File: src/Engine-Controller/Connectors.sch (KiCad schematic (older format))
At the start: 5 parts, among them P3 SBH11-PBPC-D05-RA-BK, P4 0901471110, P5 66953-005LF, U4 SN74LV07ADR

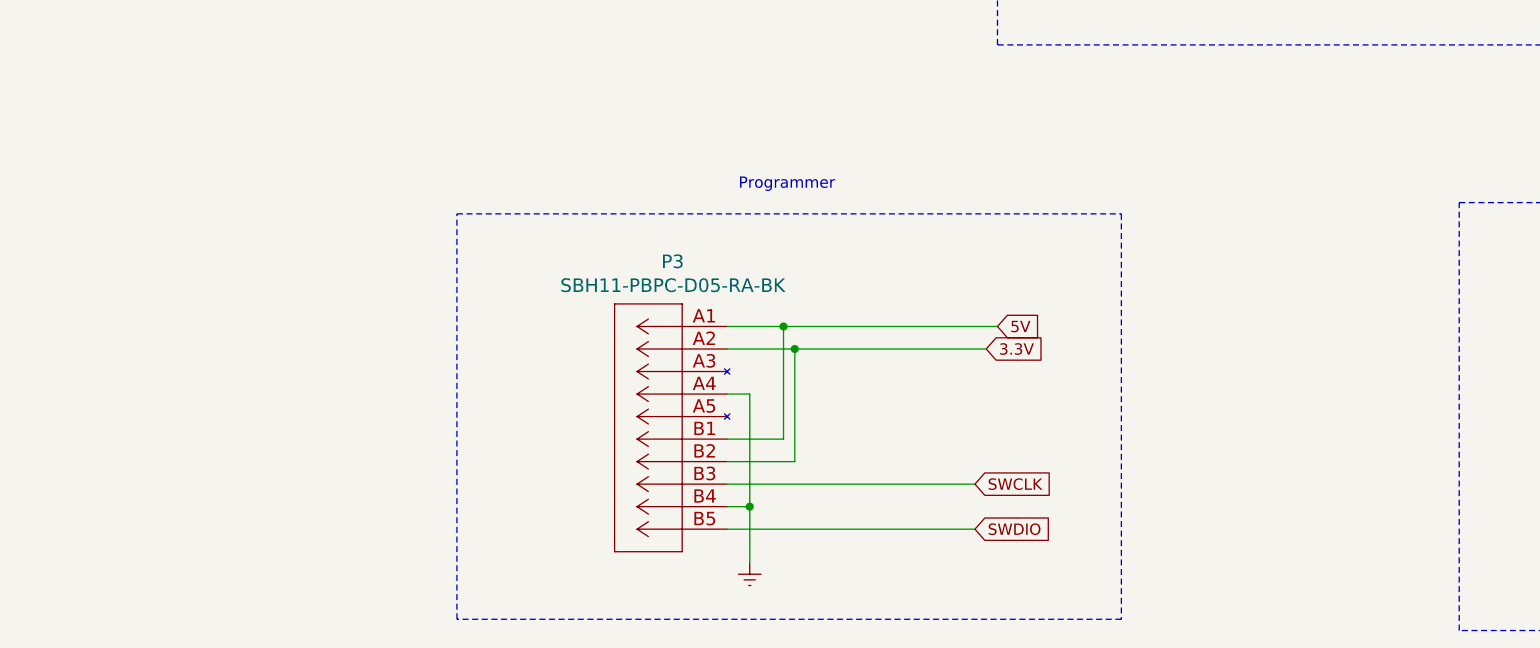
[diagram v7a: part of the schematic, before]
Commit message: Added ADC Inputs
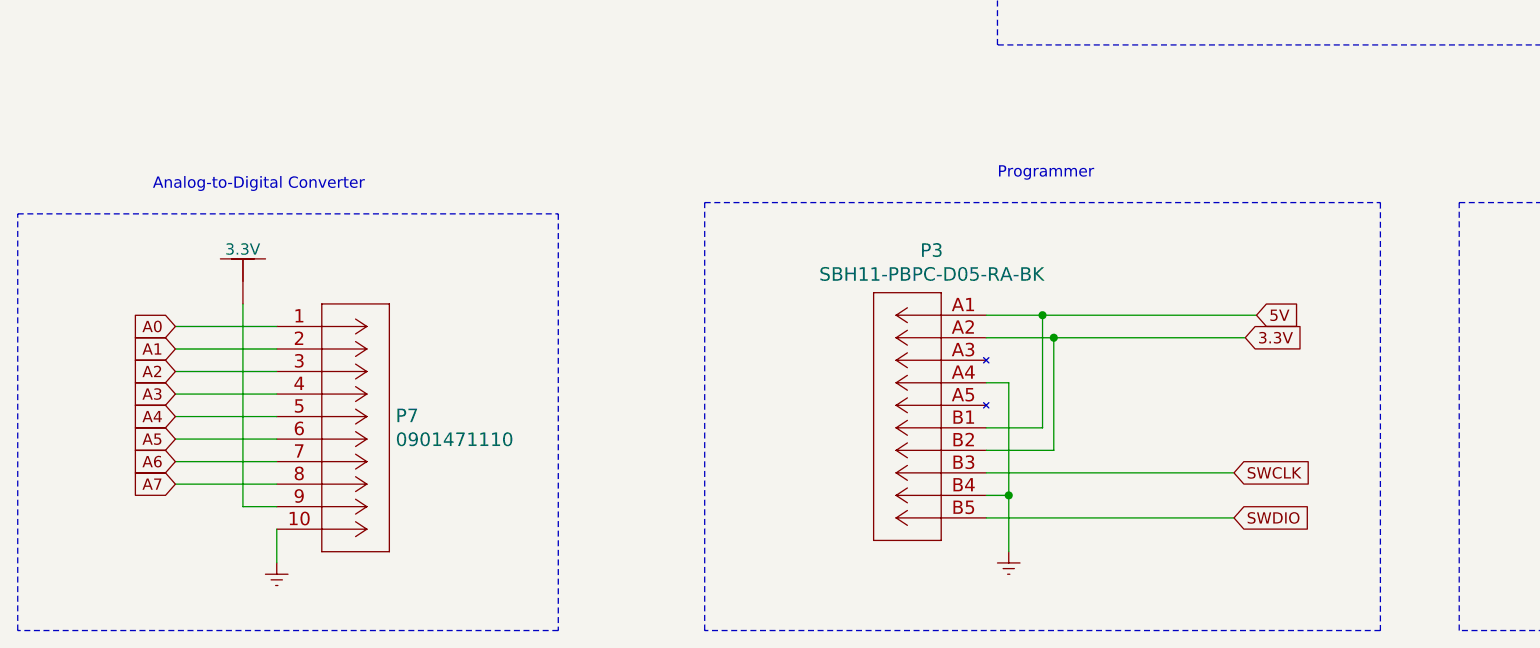
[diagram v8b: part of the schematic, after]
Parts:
- added None07: 3.3V, symbol Engine-Controller:3.3V
- added P7: 0901471110, 66953-005LF_AMP, symbol Engine-Controller:0901471110
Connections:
- net Earth: now also P7.10
- new net: None07.~, P7.9
- new net A0: P7.1
- new net A1: P7.2
- new net A2: P7.3
- new net A3: P7.4
- new net A4: P7.5
- new net A5: P7.6
- new net A6: P7.7
- new net A7: P7.8
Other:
- note added: "Analog-to-Digital Converter\n"
- moved on the sheet: P3
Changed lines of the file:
@@
 Wire Wire Line
 	8350 2850 8900 2850
-Text GLabel 5100 5150 2    50   Input ~ 0
+Text GLabel 6250 5100 2    50   Input ~ 0
 SWCLK
-Text GLabel 5100 5350 2    50   Input ~ 0
+Text GLabel 6250 5300 2    50   Input ~ 0
 SWDIO
-Text GLabel 5150 4550 2    50   Input ~ 0
+Text GLabel 6300 4500 2    50   Input ~ 0
 3.3V
-Text GLabel 5200 4450 2    50   Input ~ 0
+Text GLabel 6350 4400 2    50   Input ~ 0
 5V
 $Comp
 L power:Earth #PWR?
 U 1 1 6193D92B
-P 4100 5500
+P 5250 5450
 AR Path="/60DAAA3E/6193D92B" Ref="#PWR?"  Part="1"
 AR Path="/60E24895/6193D92B" Ref="#PWR06"  Part="1"
-F 0 "#PWR06" H 4100 5250 50  0001 C CNN
-F 1 "Earth" H 4100 5350 50  0001 C CNN
-F 2 "" H 4100 5500 50  0001 C CNN
-F 3 "~" H 4100 5500 50  0001 C CNN
-	1    4100 5500
+F 0 "#PWR06" H 5250 5200 50  0001 C CNN
+F 1 "Earth" H 5250 5300 50  0001 C CNN
+F 2 "" H 5250 5450 50  0001 C CNN
+F 3 "~" H 5250 5450 50  0001 C CNN
+	1    5250 5450
 	1    0    0    -1
 $EndComp
@@
 L Engine-Controller:SBH11-PBPC-D05-RA-BK P?
 U 1 1 6193D931
-P 4000 4450
+P 5150 4400
 AR Path="/60DAAA3E/6193D931" Ref="P?"  Part="1"
 AR Path="/60E24895/6193D931" Ref="P3"  Part="1"
-F 0 "P3" H 4242 4737 60  0000 C CNN
-F 1 "SBH11-PBPC-D05-RA-BK" H 4242 4631 60  0000 C CNN
-F 2 "66953-005LF_AMP" H 4150 3250 60  0001 C CNN
-F 3 "" H 4000 4450 60  0001 C CNN
-	1    4000 4450
+F 0 "P3" H 5392 4687 60  0000 C CNN
+F 1 "SBH11-PBPC-D05-RA-BK" H 5392 4581 60  0000 C CNN
+F 2 "66953-005LF_AMP" H 5300 3200 60  0001 C CNN
+F 3 "" H 5150 4400 60  0001 C CNN
+	1    5150 4400
 	-1   0    0    -1
 $EndComp
 Wire Wire Line
-	4000 4450 4250 4450
+	5150 4400 5400 4400
 Wire Wire Line
-	4000 4950 4250 4950
+	5150 4900 5400 4900
 Wire Wire Line
-	4250 4950 4250 4450
-Connection ~ 4250 4450
+	5400 4900 5400 4400
+Connection ~ 5400 4400
 Wire Wire Line
-	4250 4450 5200 4450
+	5400 4400 6350 4400
 Wire Wire Line
-	4000 4750 4100 4750
+	5150 4700 5250 4700
 Wire Wire Line
-	4100 4750 4100 5250
+	5250 4700 5250 5200
 Wire Wire Line
-	4000 5250 4100 5250
-Connection ~ 4100 5250
+	5150 5200 5250 5200
+Connection ~ 5250 5200
 Wire Wire Line
-	4100 5250 4100 5500
+	5250 5200 5250 5450
 Wire Wire Line
-	5150 4550 4300 4550
+	6300 4500 5450 4500
 Wire Wire Line
-	4000 5050 4300 5050
+	5150 5000 5450 5000
 Wire Wire Line
-	4300 5050 4300 4550
-Connection ~ 4300 4550
+	5450 5000 5450 4500
+Connection ~ 5450 4500
 Wire Wire Line
-	4300 4550 4000 4550
+	5450 4500 5150 4500
 Wire Wire Line
-	5100 5350 4000 5350
+	6250 5300 5150 5300
 Wire Wire Line
-	4000 5150 5100 5150
+	5150 5100 6250 5100
+Text Notes 5200 3800 0    50   ~ 0
+Programmer\n
+$Comp
+L Engine-Controller:0901471110 P7
+U 1 1 61BF9E85
+P 2000 4450
+F 0 "P7" H 2528 4053 60  0000 L CNN
+F 1 "0901471110" H 2528 3947 60  0000 L CNN
+F 2 "66953-005LF_AMP" H 2150 3250 60  0001 C CNN
+F 3 "" H 2000 4450 60  0001 C CNN
+	1    2000 4450
+	1    0    0    -1
+$EndComp
+Text GLabel 1550 4450 0    50   Input ~ 0
+A0
+Wire Wire Line
+	1550 4450 2000 4450
+Text GLabel 1550 4550 0    50   Input ~ 0
+A1
+Text GLabel 1550 4650 0    50   Input ~ 0
+A2
+Text GLabel 1550 4750 0    50   Input ~ 0
+A3
+Text GLabel 1550 4850 0    50   Input ~ 0
+A4
+Text GLabel 1550 4950 0    50   Input ~ 0
+A5
+Text GLabel 1550 5050 0    50   Input ~ 0
+A6
+Text GLabel 1550 5150 0    50   Input ~ 0
+A7
+Wire Wire Line
+	1550 4550 2000 4550
+Wire Wire Line
+	1550 4650 2000 4650
+Wire Wire Line
+	1550 4750 2000 4750
+Wire Wire Line
+	1550 4850 2000 4850
+Wire Wire Line
+	1550 4950 2000 4950
+Wire Wire Line
+	1550 5050 2000 5050
+Wire Wire Line
+	1550 5150 2000 5150
+$Comp
+L power:Earth #PWR07
+U 1 1 61C08552
+P 2000 5500
+F 0 "#PWR07" H 2000 5250 50  0001 C CNN
+F 1 "Earth" H 2000 5350 50  0001 C CNN
+F 2 "" H 2000 5500 50  0001 C CNN
+F 3 "~" H 2000 5500 50  0001 C CNN
+	1    2000 5500
+	1    0    0    -1
+$EndComp
+Wire Wire Line
+	2000 5350 2000 5500
+$Comp
+L Engine-Controller:3.3V None07
+U 1 1 61C0A50F
+P 1850 4200
+F 0 "None07" H 1978 4189 50  0001 L CNN
+F 1 "3.3V" H 1771 4292 50  0000 L CNN
+F 2 "" H 1850 4200 50  0001 C CNN
+F 3 "" H 1850 4200 50  0001 C CNN
+	1    1850 4200
+	1    0    0    -1
+$EndComp
+Wire Wire Line
+	2000 5250 1850 5250
+Wire Wire Line
+	1850 5250 1850 4350
 Wire Notes Line
-	5750 3950 5750 5750
+	6900 5800 3900 5800
 Wire Notes Line
-	5750 5750 2800 5750
+	3900 5800 3900 3900
 Wire Notes Line
-	2800 5750 2800 3950
+	3900 3900 6900 3900
 Wire Notes Line
-	2800 3950 5750 3950
-Text Notes 4050 3850 0    50   ~ 0
-Programmer\n
+	6900 3900 6900 5800
+Wire Notes Line
+	3250 3950 3250 5800
+Wire Notes Line
+	3250 5800 850  5800
+Wire Notes Line
+	850  5800 850  3950
+Wire Notes Line
+	850  3950 3250 3950
+Text Notes 1450 3850 0    50   ~ 0
+Analog-to-Digital Converter\n
 $EndSCHEMATC
